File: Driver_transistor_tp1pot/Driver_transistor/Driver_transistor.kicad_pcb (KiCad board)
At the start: 2 copper layers, 98.8 x 33.5 mm, 23 parts, among them J1 Conn_01x01, J2 Conn_01x03, J6 Conn_01x01, Q1 BC557, Q2 BC548, Q3 BC548, Q4 BU208A

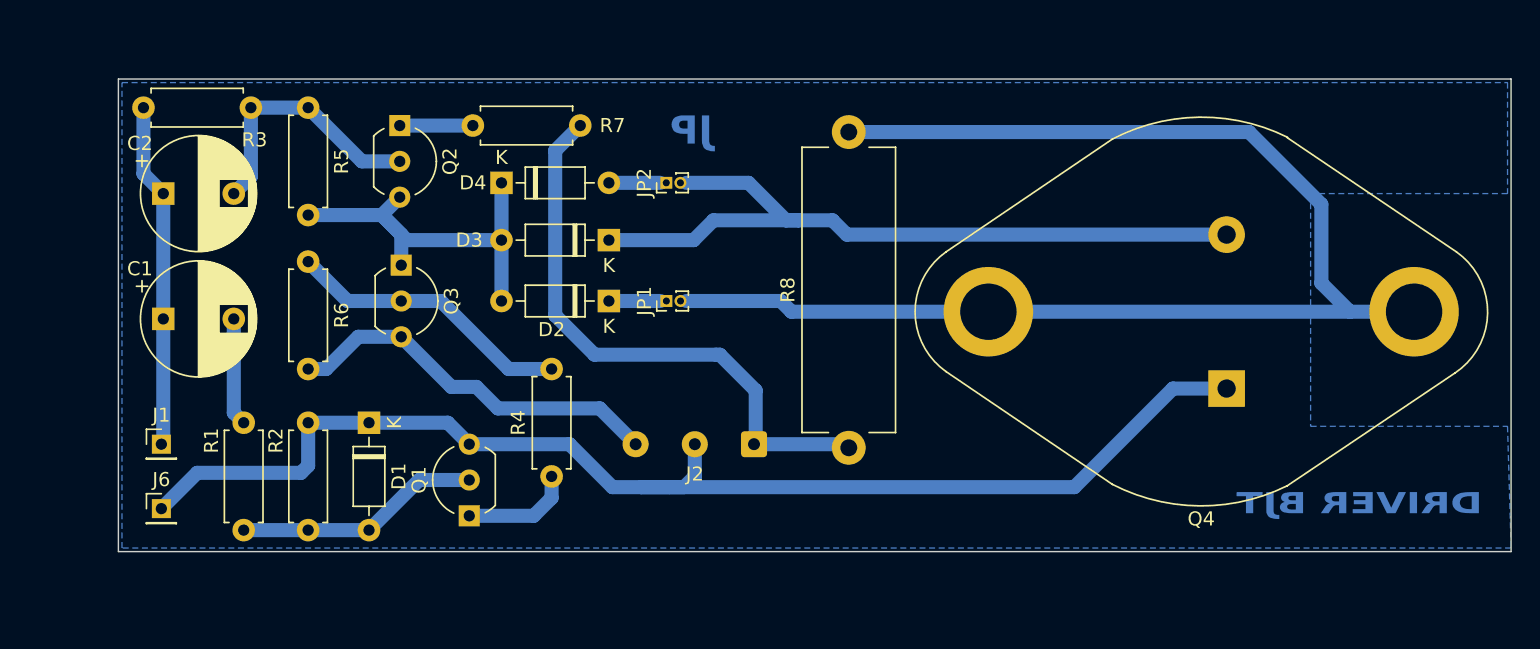
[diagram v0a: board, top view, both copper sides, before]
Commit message: rediseño driver BJT
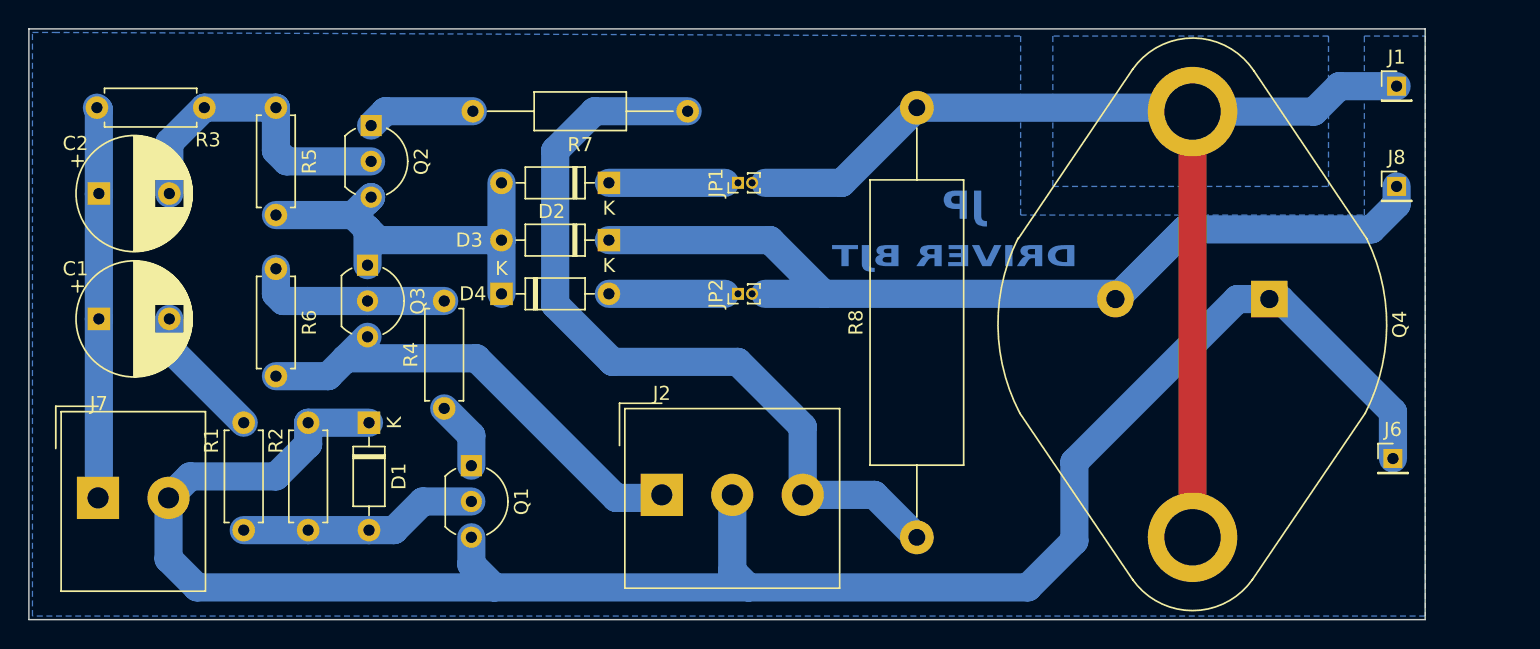
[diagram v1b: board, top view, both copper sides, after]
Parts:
- added J7: Conn_01x02, TerminalBlock_Altech:Altech_AK300_1x02_P5.00mm_45-Degree, F.Cu at (25.5, 54.6)
- added J8: base, Connector_PinHeader_2.00mm:PinHeader_1x01_P2.00mm_Vertical, F.Cu at (117.6, 32.5)
- J1: value Conn_01x01 -> colector
- J2: footprint Connector_Wire:SolderWire-0.25sqmm_1x03_P4.2mm_D0.65mm_OD1.7mm -> TerminalBlock_Altech:Altech_AK300_1x03_P5.00mm_45-Degree
- J6: value Conn_01x01 -> emisor
- R7: footprint Resistor_THT:R_Axial_DIN0207_L6.3mm_D2.5mm_P7.62mm_Horizontal -> Resistor_THT:R_Axial_DIN0207_L6.3mm_D2.5mm_P15.24mm_Horizontal
- R8: footprint Resistor_THT:R_Axial_Power_L20.0mm_W6.4mm_P22.40mm -> Resistor_THT:R_Axial_Power_L20.0mm_W6.4mm_P30.48mm
- moved J1 91.2 mm to (117.6, 25.4)
- moved J6 87.4 mm to (117.3, 51.8)
- moved JP1 9.80 mm to (70.9, 32.3)
- moved JP2 9.37 mm to (70.9, 40.1)
- moved R4 9.02 mm to (50.0, 48.3)
- moved D2 8.38 mm to (61.7, 32.3)
- moved R8 7.98 mm to (83.6, 57.4)
- moved D4 7.87 mm to (54.1, 40.1)
- moved R7 7.69 mm to (67.3, 27.2)
- moved J2 7.47 mm to (65.5, 54.4), turned to 0 degrees
- moved Q4 7.04 mm to (108.6, 40.5), turned to -90 degrees
- moved C1 4.57 mm to (25.5, 41.9)
- moved C2 4.57 mm to (25.5, 33.0)
- moved Q1 3.56 mm to (52.0, 52.3), turned to -90 degrees
- moved R3 3.30 mm to (25.4, 26.9)
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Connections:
- J1 pad 1: pwm -> colector
- J2 pad 1: +12V -> -12V
- J2 pad 3: -12V -> +12V
- JP1 pad 2: Net-(JP1-B) -> colector
- Q4 pad 3: Net-(JP1-B) -> colector
- R8 pad 2: Net-(JP1-B) -> colector
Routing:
- net Net-(JP1-B): track 96.0 -> 0.00 mm
- net colector: track 0.00 -> 78.1 mm
- net GND: track 91.1 -> 139.0 mm
- net Net-(D3-K): track 53.9 -> 72.5 mm
- net +12V: track 41.3 -> 56.8 mm
- net -12V: track 27.3 -> 34.4 mm
- net Net-(Q3-B): track 20.4 -> 13.9 mm
- net Net-(D4-A): track 3.65 -> 8.23 mm
- net Net-(D2-K): track 3.65 -> 8.23 mm
- net Net-(Q2-B): track 18.7 -> 22.3 mm
- net pwm: track 24.5 -> 27.8 mm
- net Net-(Q1-C): track 7.89 -> 4.86 mm
- net Net-(Q2-C): track 5.19 -> 7.64 mm
- net Net-(C1-Pad2): track 7.66 -> 9.55 mm
- net Net-(D2-A): track 28.8 -> 29.3 mm
- added copper zone on B.Cu, net colector
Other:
- board size 98.8 x 33.5 mm -> 99.1 x 41.9 mm
